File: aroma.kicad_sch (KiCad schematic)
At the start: 0 parts

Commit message: v1
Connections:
- no-connect marks 0 -> 4
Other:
- sheet Externals ports: added LED, MIST; removed none
- sheet MCU ports: added IO12, IO13, IO14, IO15, IO2, IO25, IO26, IO27; removed none

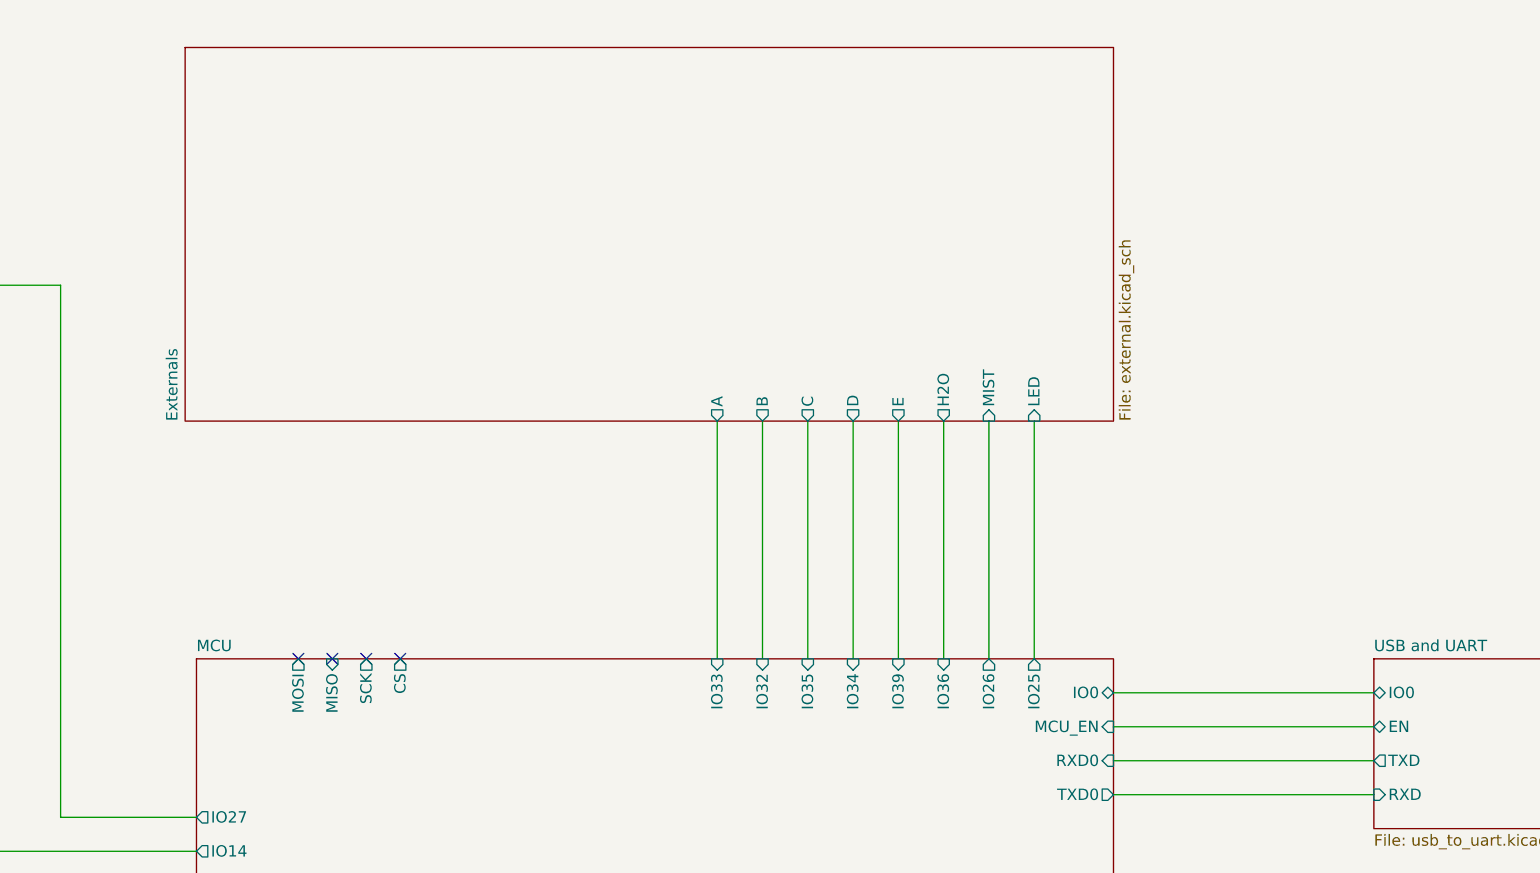
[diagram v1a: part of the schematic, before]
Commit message: LCD Display
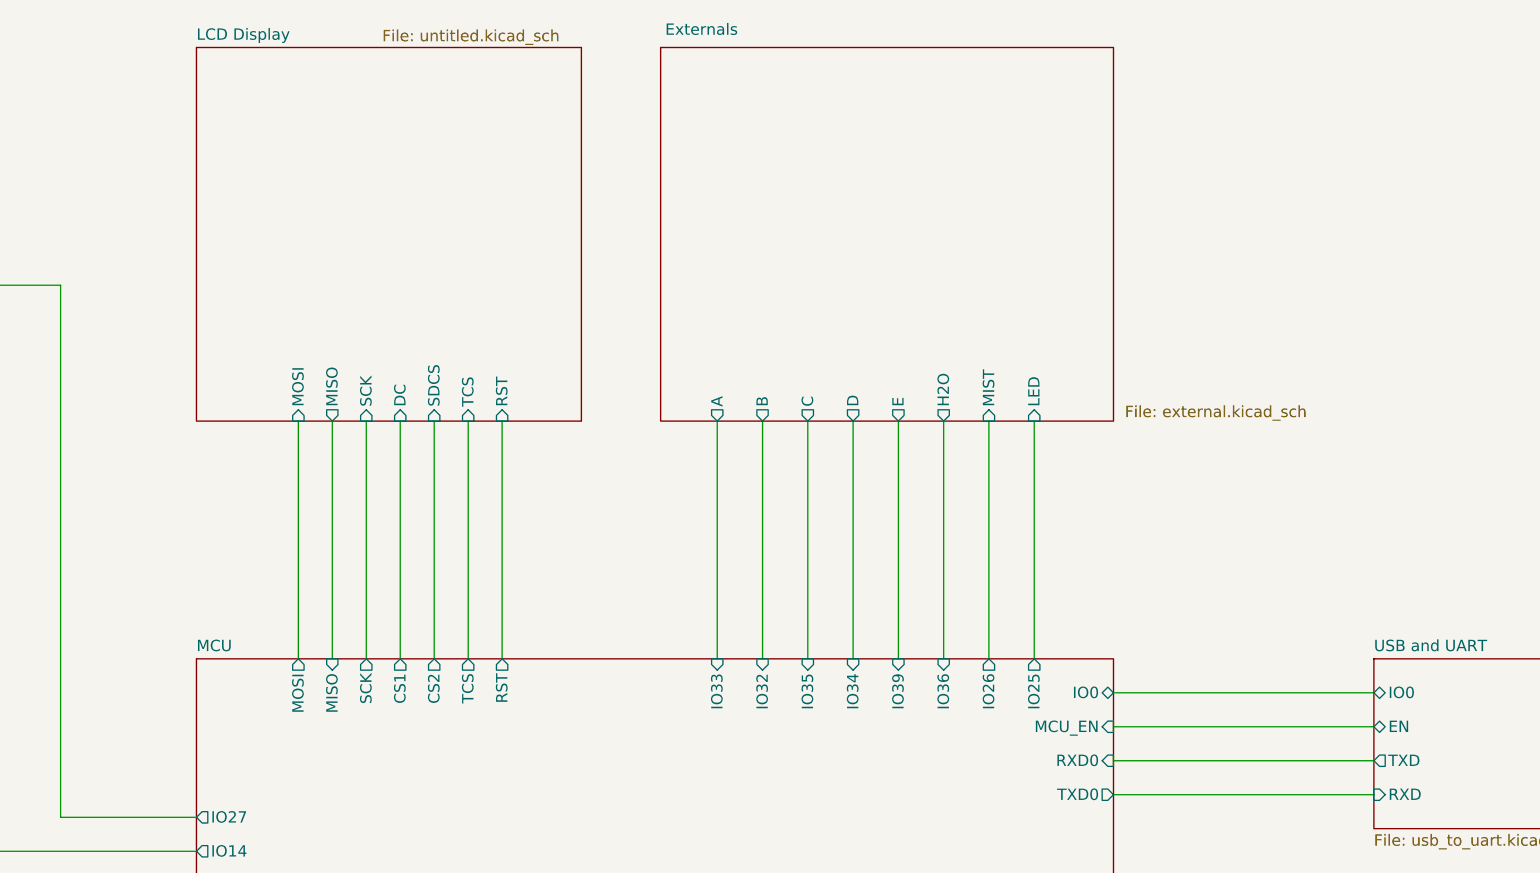
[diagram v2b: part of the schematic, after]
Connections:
- no-connect marks 4 -> 0
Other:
- added sheet LCD Display (untitled.kicad_sch)
- sheet MCU ports: added CS1, CS2, RST, TCS; removed CS
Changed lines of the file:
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@@
 	(generator_version "8.0")
 	(paper "A4")
-	(no_connect
-		(at 119.38 97.79)
-	)
-	(no_connect
-		(at 123.19 97.79)
-	)
-	(no_connect
-		(at 111.76 97.79)
-	)
-	(no_connect
-		(at 115.57 97.79)
-	)
 	(wire
 		(pts
@@
 	(wire
 		(pts
+			(xy 127 71.12) (xy 127 97.79)
+		)
+		(stroke
+			(width 0)
+			(type default)
+		)
+	)
+	(wire
+		(pts
 			(xy 203.2 101.6) (xy 232.41 101.6)
 		)
@@
 	(wire
 		(pts
+			(xy 130.81 71.12) (xy 130.81 97.79)
+		)
+		(stroke
+			(width 0)
+			(type default)
+		)
+	)
+	(wire
+		(pts
+			(xy 134.62 71.12) (xy 134.62 97.79)
+		)
+		(stroke
+			(width 0)
+			(type default)
+		)
+	)
+	(wire
+		(pts
 			(xy 189.23 71.12) (xy 189.23 97.79)
 		)
@@
 	(wire
 		(pts
+			(xy 115.57 71.12) (xy 115.57 97.79)
+		)
+		(stroke
+			(width 0)
+			(type default)
+		)
+	)
+	(wire
+		(pts
 			(xy 179.07 71.12) (xy 179.07 97.79)
 		)
@@
 	(wire
 		(pts
+			(xy 111.76 71.12) (xy 111.76 97.79)
+		)
+		(stroke
+			(width 0)
+			(type default)
+		)
+	)
+	(wire
+		(pts
 			(xy 100.33 130.81) (xy 78.74 130.81)
 		)
@@
 	(wire
 		(pts
+			(xy 119.38 71.12) (xy 119.38 97.79)
+		)
+		(stroke
+			(width 0)
+			(type default)
+		)
+	)
+	(wire
+		(pts
 			(xy 67.31 93.98) (xy 67.31 123.19)
+		)
+		(stroke
+			(width 0)
+			(type default)
+		)
+	)
+	(wire
+		(pts
+			(xy 123.19 71.12) (xy 123.19 97.79)
 		)
 		(stroke
@@
 			(project "aroma"
 				(path "/41d97073-34b5-4be3-afd3-c3d0ba6d78a9"
-					(page "8")
+					(page "9")
 				)
 			)
@@
 			(project "aroma"
 				(path "/41d97073-34b5-4be3-afd3-c3d0ba6d78a9"
-					(page "7")
+					(page "8")
 				)
 			)
@@
 			(project "aroma"
 				(path "/41d97073-34b5-4be3-afd3-c3d0ba6d78a9"
-					(page "9")
+					(page "10")
 				)
 			)
@@
 	)
 	(sheet
-		(at 99.06 29.21)
-		(size 104.14 41.91)
-		(fields_autoplaced yes)
+		(at 152.4 29.21)
+		(size 50.8 41.91)
 		(stroke
 			(width 0.1524)
@@
 		)
 		(property "Sheetname" "Externals"
-			(at 98.3484 71.12 90)
+			(at 152.908 27.94 0)
 			(effects
 				(font
@@
 		)
 		(property "Sheetfile" "external.kicad_sch"
-			(at 203.7846 71.12 90)
+			(at 204.47 69.342 0)
 			(effects
 				(font
@@
 			)
 		)
-		(pin "CS" output
-			(at 123.19 97.79 90)
-			(effects
-				(font
-					(size 1.27 1.27)
-				)
-				(justify right)
-			)
-		)
 		(pin "IO39" input
 			(at 179.07 97.79 90)
@@
 		(pin "IO25" output
 			(at 194.31 97.79 90)
+			(effects
+				(font
+					(size 1.27 1.27)
+				)
+				(justify right)
+			)
+		)
+		(pin "CS1" output
+			(at 123.19 97.79 90)
+			(effects
+				(font
+					(size 1.27 1.27)
+				)
+				(justify right)
+			)
+		)
+		(pin "CS2" output
+			(at 127 97.79 90)
+			(effects
+				(font
+					(size 1.27 1.27)
+				)
+				(justify right)
+			)
+		)
+		(pin "TCS" output
+			(at 130.81 97.79 90)
+			(effects
+				(font
+					(size 1.27 1.27)
+				)
+				(justify right)
+			)
+		)
+		(pin "RST" output
+			(at 134.62 97.79 90)
 			(effects
 				(font
@@
 			(project "aroma"
 				(path "/41d97073-34b5-4be3-afd3-c3d0ba6d78a9"
+					(page "7")
+				)
+			)
+		)
+	)
+	(sheet
+		(at 100.33 29.21)
+		(size 43.18 41.91)
+		(stroke
+			(width 0.1524)
+			(type solid)
+		)
+		(fill
+			(color 0 0 0 0.0000)
+		)
+		(property "Sheetname" "LCD Display"
+			(at 100.33 28.4984 0)
+			(effects
+				(font
+					(size 1.27 1.27)
+				)
+				(justify left bottom)
+			)
+		)
+		(property "Sheetfile" "untitled.kicad_sch"
+			(at 121.158 27.178 0)
+			(effects
+				(font
+					(size 1.27 1.27)
+				)
+				(justify left top)
+			)
+		)
+		(pin "MOSI" input
+			(at 111.76 71.12 270)
+			(effects
+				(font
+					(size 1.27 1.27)
+				)
+				(justify left)
+			)
+		)
+		(pin "TCS" input
+			(at 130.81 71.12 270)
+			(effects
+				(font
+					(size 1.27 1.27)
+				)
+				(justify left)
+			)
+		)
+		(pin "RST" input
+			(at 134.62 71.12 270)
+			(effects
+				(font
+					(size 1.27 1.27)
+				)
+				(justify left)
+			)
+		)
+		(pin "DC" input
+			(at 123.19 71.12 270)
+			(effects
+				(font
+					(size 1.27 1.27)
+				)
+				(justify left)
+			)
+		)
+		(pin "SDCS" input
+			(at 127 71.12 270)
+			(effects
+				(font
+					(size 1.27 1.27)
+				)
+				(justify left)
+			)
+		)
+		(pin "SCK" input
+			(at 119.38 71.12 270)
+			(effects
+				(font
+					(size 1.27 1.27)
+				)
+				(justify left)
+			)
+		)
+		(pin "MISO" output
+			(at 115.57 71.12 270)
+			(effects
+				(font
+					(size 1.27 1.27)
+				)
+				(justify left)
+			)
+		)
+		(instances
+			(project "aroma"
+				(path "/41d97073-34b5-4be3-afd3-c3d0ba6d78a9"
 					(page "6")
 				)
@@
 			(project "aroma"
 				(path "/41d97073-34b5-4be3-afd3-c3d0ba6d78a9"
-					(page "11")
+					(page "12")
 				)
 			)
@@
 			(project "aroma"
 				(path "/41d97073-34b5-4be3-afd3-c3d0ba6d78a9"
-					(page "10")
-				)
-			)
+					(page "11")
+				)
+			)

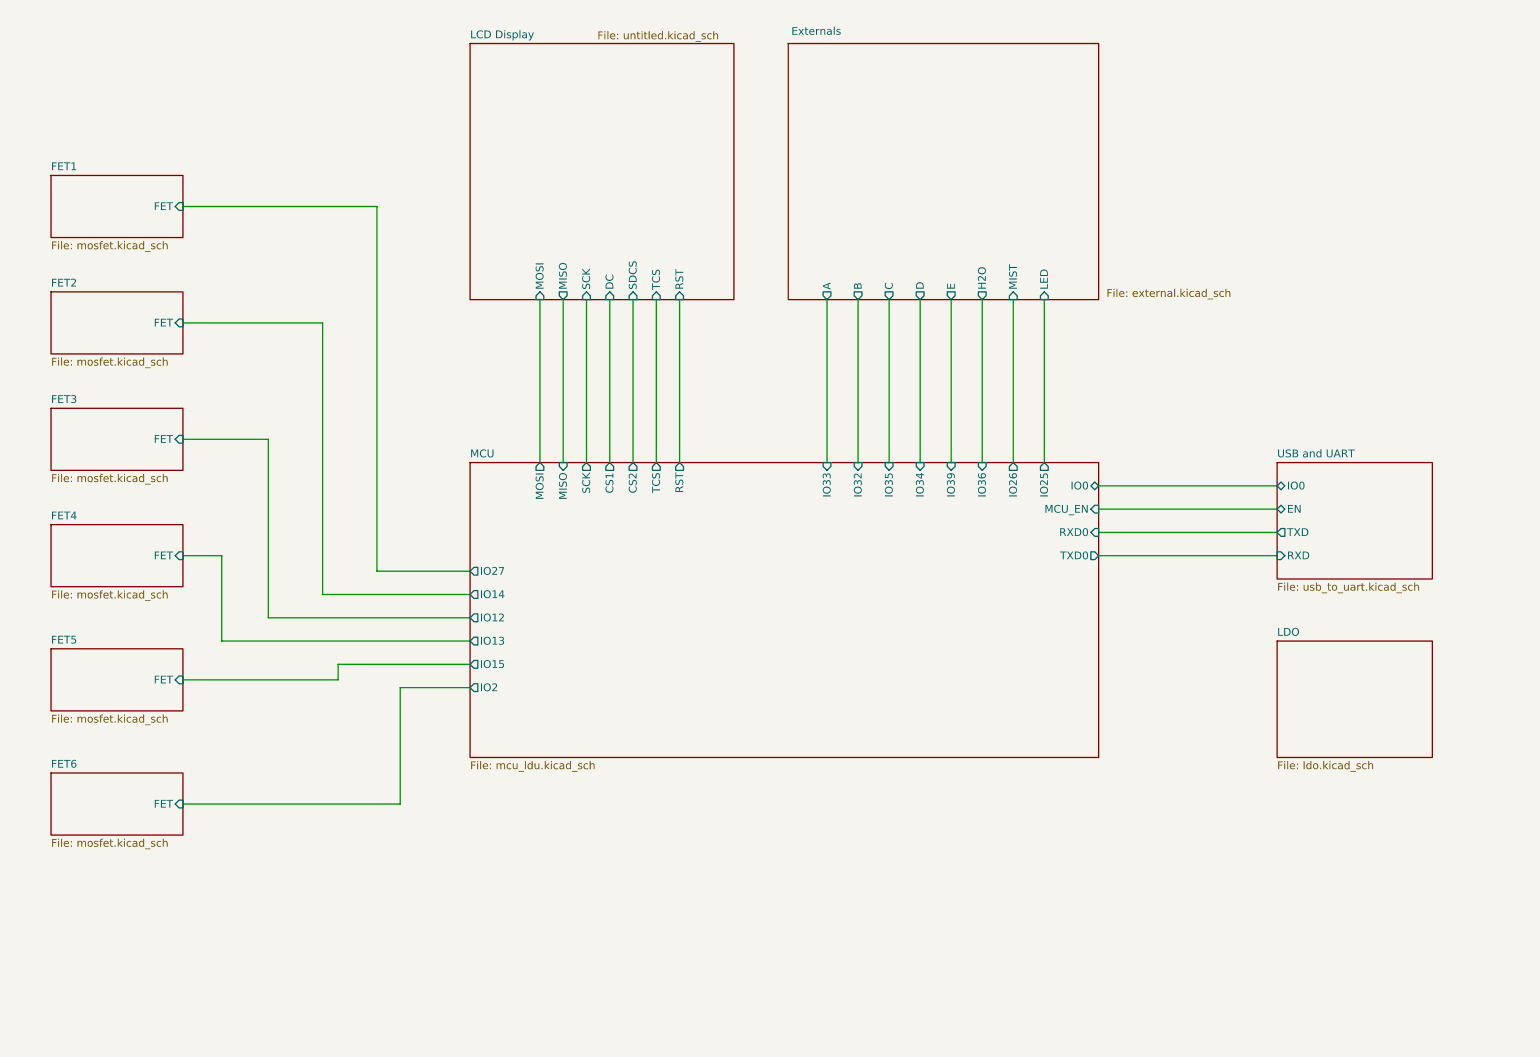
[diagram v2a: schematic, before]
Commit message: passed drc (somehow)
board routing is def cooked
verify:
- boost layout
- usb terminal layout
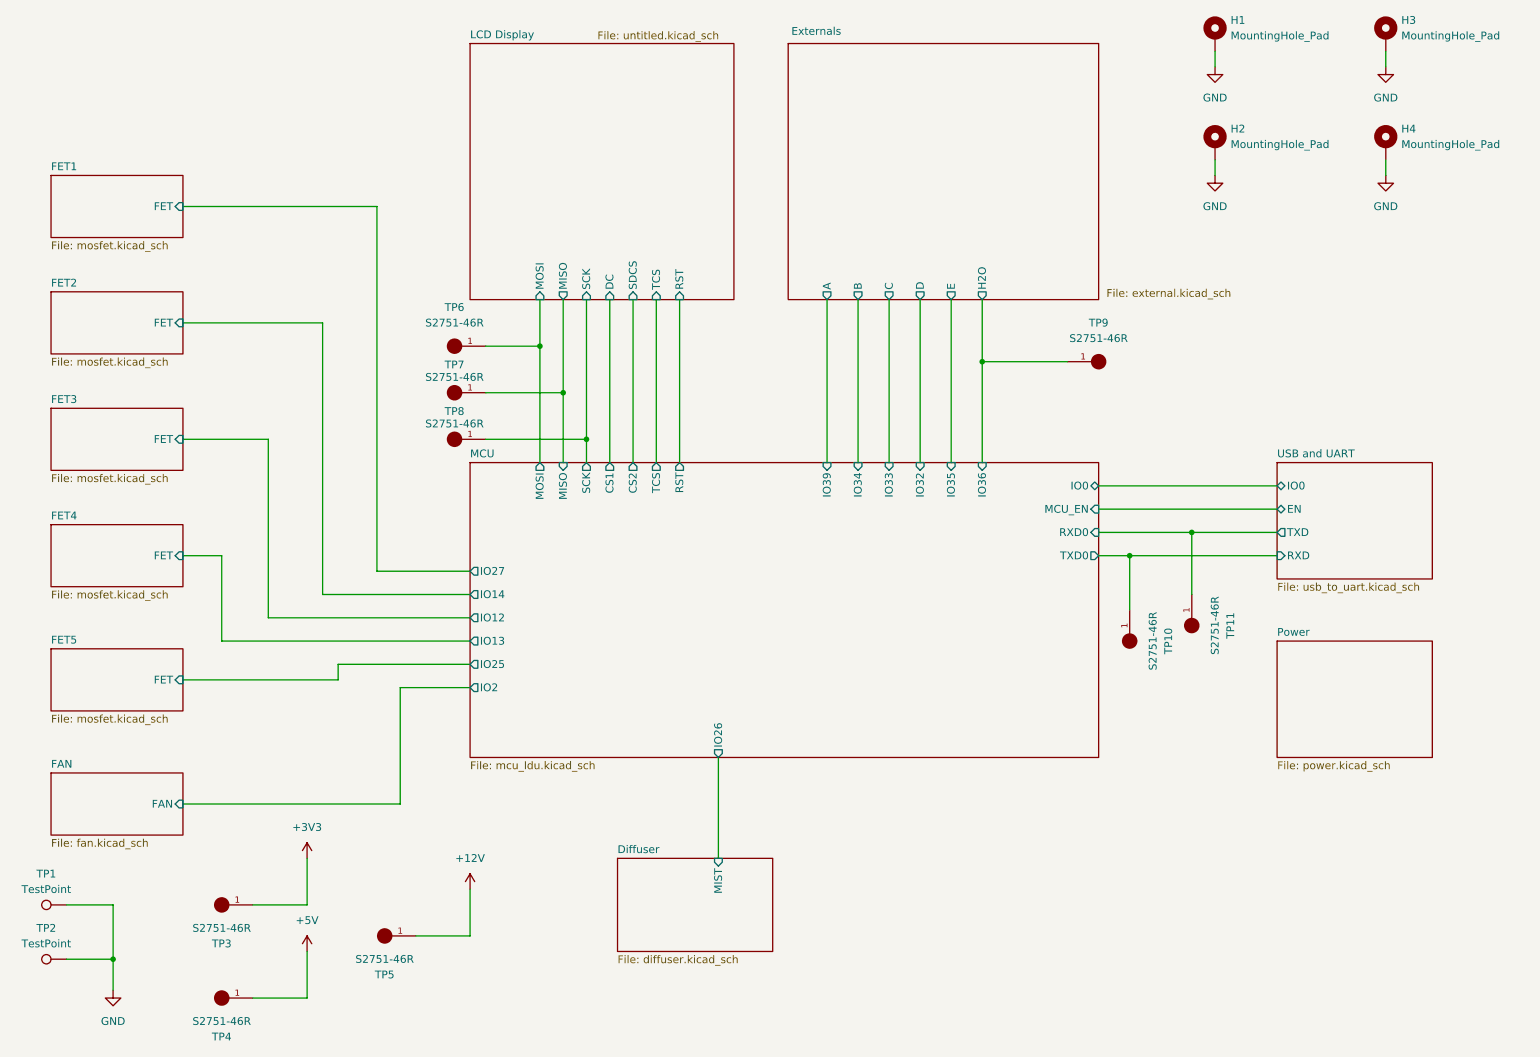
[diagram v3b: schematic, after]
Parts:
- added H1, H2, H3, H4: MountingHole_Pad, MountingHole:MountingHole_3.5mm_Pad, symbol Mechanical:MountingHole_Pad
- added TP1, TP2: TestPoint, TestPoint:TestPoint_THTPad_2.0x2.0mm_Drill1.0mm, symbol Connector:TestPoint
- added TP10, TP11, TP3, TP4, TP5, TP6, TP7, TP8, TP9: S2751-46R, footprints:S2751-46R, symbol S2751-46R:S2751-46R
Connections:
- net Externals/H2O: now also TP9.1
- net LCD Display/MISO: now also TP7.1
- net LCD Display/MOSI: now also TP6.1
- net LCD Display/SCK: now also TP8.1
- net MCU/RXD0: now also TP11.1
- net MCU/TXD0: now also TP10.1
- new net +12V: TP5.1
- new net +3V3: TP3.1
- new net +5V: TP4.1
- new net GND: H1.1, H2.1, H3.1, H4.1, TP1.1, TP2.1
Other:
- sheet LDO renamed Power
- removed sheet FET6
- added sheet Diffuser (diffuser.kicad_sch)
- added sheet FAN (fan.kicad_sch)
- sheet Externals ports: added none; removed LED, MIST
- sheet MCU ports: added none; removed IO15
- sheet Power: file ldo.kicad_sch -> power.kicad_sch
